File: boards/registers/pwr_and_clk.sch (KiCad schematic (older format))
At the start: 17 parts, among them J4 5V, SW1 RESET, SW2 STEP, SW3 STEP/RUN, U34 74ACT14

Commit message: Fixed some footprints
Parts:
- C37: footprint LED_SMD:LED_0805_2012Metric -> Capacitor_SMD:C_0805_2012Metric
- C38: footprint LED_SMD:LED_0805_2012Metric -> Capacitor_SMD:CP_Elec_4x4.5
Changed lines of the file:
@@
 F 0 "C38" H 9118 1396 50  0000 L CNN
 F 1 "100u" H 9118 1305 50  0000 L CNN
-F 2 "LED_SMD:LED_0805_2012Metric" H 9038 1200 50  0001 C CNN
+F 2 "Capacitor_SMD:CP_Elec_4x4.5" H 9038 1200 50  0001 C CNN
 F 3 "~" H 9000 1350 50  0001 C CNN
 	1    9000 1350
@@
 F 0 "C37" H 7665 4496 50  0000 L CNN
 F 1 "0.1u" H 7665 4405 50  0000 L CNN
-F 2 "LED_SMD:LED_0805_2012Metric" H 7588 4300 50  0001 C CNN
+F 2 "Capacitor_SMD:C_0805_2012Metric" H 7588 4300 50  0001 C CNN
 F 3 "~" H 7550 4450 50  0001 C CNN
 	1    7550 4450
@@
 	2650 2400 2650 1750
 $Comp
-L power:GND #PWR?
+L power:GND #PWR0101
 U 1 1 5FBA3876
 P 2000 3000
-F 0 "#PWR?" H 2000 2750 50  0001 C CNN
+F 0 "#PWR0101" H 2000 2750 50  0001 C CNN
 F 1 "GND" V 2005 2872 50  0000 R CNN
 F 2 "" H 2000 3000 50  0001 C CNN
@@
 $EndComp
 $Comp
-L power:GND #PWR?
+L power:GND #PWR0106
 U 1 1 5FBA3DBF
 P 2050 4400
-F 0 "#PWR?" H 2050 4150 50  0001 C CNN
+F 0 "#PWR0106" H 2050 4150 50  0001 C CNN
 F 1 "GND" V 2055 4272 50  0000 R CNN
 F 2 "" H 2050 4400 50  0001 C CNN
@@
 Connection ~ 2850 3000
 $Comp
-L power:VCC #PWR?
+L power:VCC #PWR0107
 U 1 1 5FBA8516
 P 2650 2700
-F 0 "#PWR?" H 2650 2550 50  0001 C CNN
+F 0 "#PWR0107" H 2650 2550 50  0001 C CNN
 F 1 "VCC" H 2667 2873 50  0000 C CNN
 F 2 "" H 2650 2700 50  0001 C CNN
@@
 $EndComp
 $Comp
-L power:VCC #PWR?
+L power:VCC #PWR0124
 U 1 1 5FBA8A47
 P 2850 2700
-F 0 "#PWR?" H 2850 2550 50  0001 C CNN
+F 0 "#PWR0124" H 2850 2550 50  0001 C CNN
 F 1 "VCC" H 2867 2873 50  0000 C CNN
 F 2 "" H 2850 2700 50  0001 C CNN

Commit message: Part names
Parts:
- SW3: value STEP/RUN -> OS102011MS2QN1
- U34: value 74ACT14 -> 74ACT14MTCX
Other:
- note added: "RESET"
- note added: "STEP"
- note added: "STEP/RUN"
- moved on the sheet: C37
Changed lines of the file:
@@
 P 3550 1750
 F 0 "U34" H 3550 2067 50  0000 C CNN
-F 1 "74ACT14" H 3550 1976 50  0000 C CNN
+F 1 "74ACT14MTCX" H 3550 1976 50  0000 C CNN
 F 2 "Package_SO:TSSOP-14_4.4x5mm_P0.65mm" H 3550 1750 50  0001 C CNN
 F 3 "http://www.ti.com/lit/gpn/sn74HC14" H 3550 1750 50  0001 C CNN
@@
 P 4950 1750
 F 0 "U34" H 4950 2067 50  0000 C CNN
-F 1 "74ACT14" H 4950 1976 50  0000 C CNN
+F 1 "74ACT14MTCX" H 4950 1976 50  0000 C CNN
 F 2 "Package_SO:TSSOP-14_4.4x5mm_P0.65mm" H 4950 1750 50  0001 C CNN
 F 3 "http://www.ti.com/lit/gpn/sn74HC14" H 4950 1750 50  0001 C CNN
@@
 P 5550 1750
 F 0 "U34" H 5550 2067 50  0000 C CNN
-F 1 "74ACT14" H 5550 1976 50  0000 C CNN
+F 1 "74ACT14MTCX" H 5550 1976 50  0000 C CNN
 F 2 "Package_SO:TSSOP-14_4.4x5mm_P0.65mm" H 5550 1750 50  0001 C CNN
 F 3 "http://www.ti.com/lit/gpn/sn74HC14" H 5550 1750 50  0001 C CNN
@@
 P 3550 3000
 F 0 "U34" H 3550 3317 50  0000 C CNN
-F 1 "74ACT14" H 3550 3226 50  0000 C CNN
+F 1 "74ACT14MTCX" H 3550 3226 50  0000 C CNN
 F 2 "Package_SO:TSSOP-14_4.4x5mm_P0.65mm" H 3550 3000 50  0001 C CNN
 F 3 "http://www.ti.com/lit/gpn/sn74HC14" H 3550 3000 50  0001 C CNN
@@
 P 3550 4400
 F 0 "U34" H 3550 4717 50  0000 C CNN
-F 1 "74ACT14" H 3550 4626 50  0000 C CNN
+F 1 "74ACT14MTCX" H 3550 4626 50  0000 C CNN
 F 2 "Package_SO:TSSOP-14_4.4x5mm_P0.65mm" H 3550 4400 50  0001 C CNN
 F 3 "http://www.ti.com/lit/gpn/sn74HC14" H 3550 4400 50  0001 C CNN
@@
 U 1 1 5EF35857
 P 4450 1750
-F 0 "SW3" H 4450 1425 50  0000 C CNN
-F 1 "STEP/RUN" H 4450 1516 50  0000 C CNN
+F 0 "SW3" H 4500 2000 50  0000 C CNN
+F 1 "OS102011MS2QN1" H 4250 2100 50  0000 C CNN
 F 2 "Button_Switch_THT:SW_Slide_1P2T_CK_OS102011MS2Q" H 4450 1750 50  0001 C CNN
 F 3 "~" H 4450 1750 50  0001 C CNN
@@
 P 4800 3000
 F 0 "U34" H 4800 3317 50  0000 C CNN
-F 1 "74ACT14" H 4800 3226 50  0000 C CNN
+F 1 "74ACT14MTCX" H 4800 3226 50  0000 C CNN
 F 2 "Package_SO:TSSOP-14_4.4x5mm_P0.65mm" H 4800 3000 50  0001 C CNN
 F 3 "http://www.ti.com/lit/gpn/sn74HC14" H 4800 3000 50  0001 C CNN
@@
 P 6800 4450
 F 0 "U34" H 7030 4496 50  0000 L CNN
-F 1 "74ACT14" H 7030 4405 50  0000 L CNN
+F 1 "74ACT14MTCX" H 7030 4405 50  0000 L CNN
 F 2 "Package_SO:TSSOP-14_4.4x5mm_P0.65mm" H 6800 4450 50  0001 C CNN
 F 3 "http://www.ti.com/lit/gpn/sn74HC14" H 6800 4450 50  0001 C CNN
@@
 L Device:C C37
 U 1 1 5EF50873
-P 7550 4450
-F 0 "C37" H 7665 4496 50  0000 L CNN
-F 1 "0.1u" H 7665 4405 50  0000 L CNN
-F 2 "Capacitor_SMD:C_0805_2012Metric" H 7588 4300 50  0001 C CNN
-F 3 "~" H 7550 4450 50  0001 C CNN
-	1    7550 4450
+P 7700 4450
+F 0 "C37" H 7815 4496 50  0000 L CNN
+F 1 "0.1u" H 7815 4405 50  0000 L CNN
+F 2 "Capacitor_SMD:C_0805_2012Metric" H 7738 4300 50  0001 C CNN
+F 3 "~" H 7700 4450 50  0001 C CNN
+	1    7700 4450
 	1    0    0    -1
 $EndComp
@@
 L power:GND #PWR0228
 U 1 1 5EF50EFD
-P 7550 4600
-F 0 "#PWR0228" H 7550 4350 50  0001 C CNN
-F 1 "GND" H 7555 4427 50  0000 C CNN
-F 2 "" H 7550 4600 50  0001 C CNN
-F 3 "" H 7550 4600 50  0001 C CNN
-	1    7550 4600
+P 7700 4600
+F 0 "#PWR0228" H 7700 4350 50  0001 C CNN
+F 1 "GND" H 7705 4427 50  0000 C CNN
+F 2 "" H 7700 4600 50  0001 C CNN
+F 3 "" H 7700 4600 50  0001 C CNN
+	1    7700 4600
 	1    0    0    -1
 $EndComp
@@
 L power:VCC #PWR0227
 U 1 1 5EF5151C
-P 7550 4300
-F 0 "#PWR0227" H 7550 4150 50  0001 C CNN
-F 1 "VCC" H 7567 4473 50  0000 C CNN
-F 2 "" H 7550 4300 50  0001 C CNN
-F 3 "" H 7550 4300 50  0001 C CNN
-	1    7550 4300
+P 7700 4300
+F 0 "#PWR0227" H 7700 4150 50  0001 C CNN
+F 1 "VCC" H 7717 4473 50  0000 C CNN
+F 2 "" H 7700 4300 50  0001 C CNN
+F 3 "" H 7700 4300 50  0001 C CNN
+	1    7700 4300
 	1    0    0    -1
 $EndComp
@@
 	2400 3000 2650 3000
 Connection ~ 2650 3000
+Text Notes 4550 1600 2    50   ~ 0
+STEP/RUN
+Text Notes 2300 3150 2    50   ~ 0
+RESET
+Text Notes 2350 4550 2    50   ~ 0
+STEP
 $EndSCHEMATC

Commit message: Power connector on the IO board
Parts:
- removed J4: 5V, Connector_PinHeader_2.54mm:PinHeader_1x02_P2.54mm_Vertical, symbol Connector_Generic:Conn_01x02
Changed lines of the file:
@@
-$EndComp
-$Comp
-L Connector_Generic:Conn_01x02 J4
-U 1 1 5EF4AAE6
-P 8250 1400
-F 0 "J4" H 8600 1250 50  0000 C CNN
-F 1 "5V" H 8600 1400 50  0000 C CNN
-F 2 "Connector_PinHeader_2.54mm:PinHeader_1x02_P2.54mm_Vertical" H 8250 1400 50  0001 C CNN
-F 3 "~" H 8250 1400 50  0001 C CNN
-	1    8250 1400
-	-1   0    0    1
-$EndComp
-$Comp
-L power:GND #PWR0230
-U 1 1 5EF4B86D
-P 8450 1400
-F 0 "#PWR0230" H 8450 1150 50  0001 C CNN
-F 1 "GND" H 8455 1227 50  0000 C CNN
-F 2 "" H 8450 1400 50  0001 C CNN
-F 3 "" H 8450 1400 50  0001 C CNN
-	1    8450 1400
-	1    0    0    -1
-$EndComp
-$Comp
-L power:VCC #PWR0229
-U 1 1 5EF4BF47
-P 8450 1300
-F 0 "#PWR0229" H 8450 1150 50  0001 C CNN
-F 1 "VCC" H 8467 1473 50  0000 C CNN
-F 2 "" H 8450 1300 50  0001 C CNN
-F 3 "" H 8450 1300 50  0001 C CNN
-	1    8450 1300
-	1    0    0    -1
 $EndComp
 $Comp

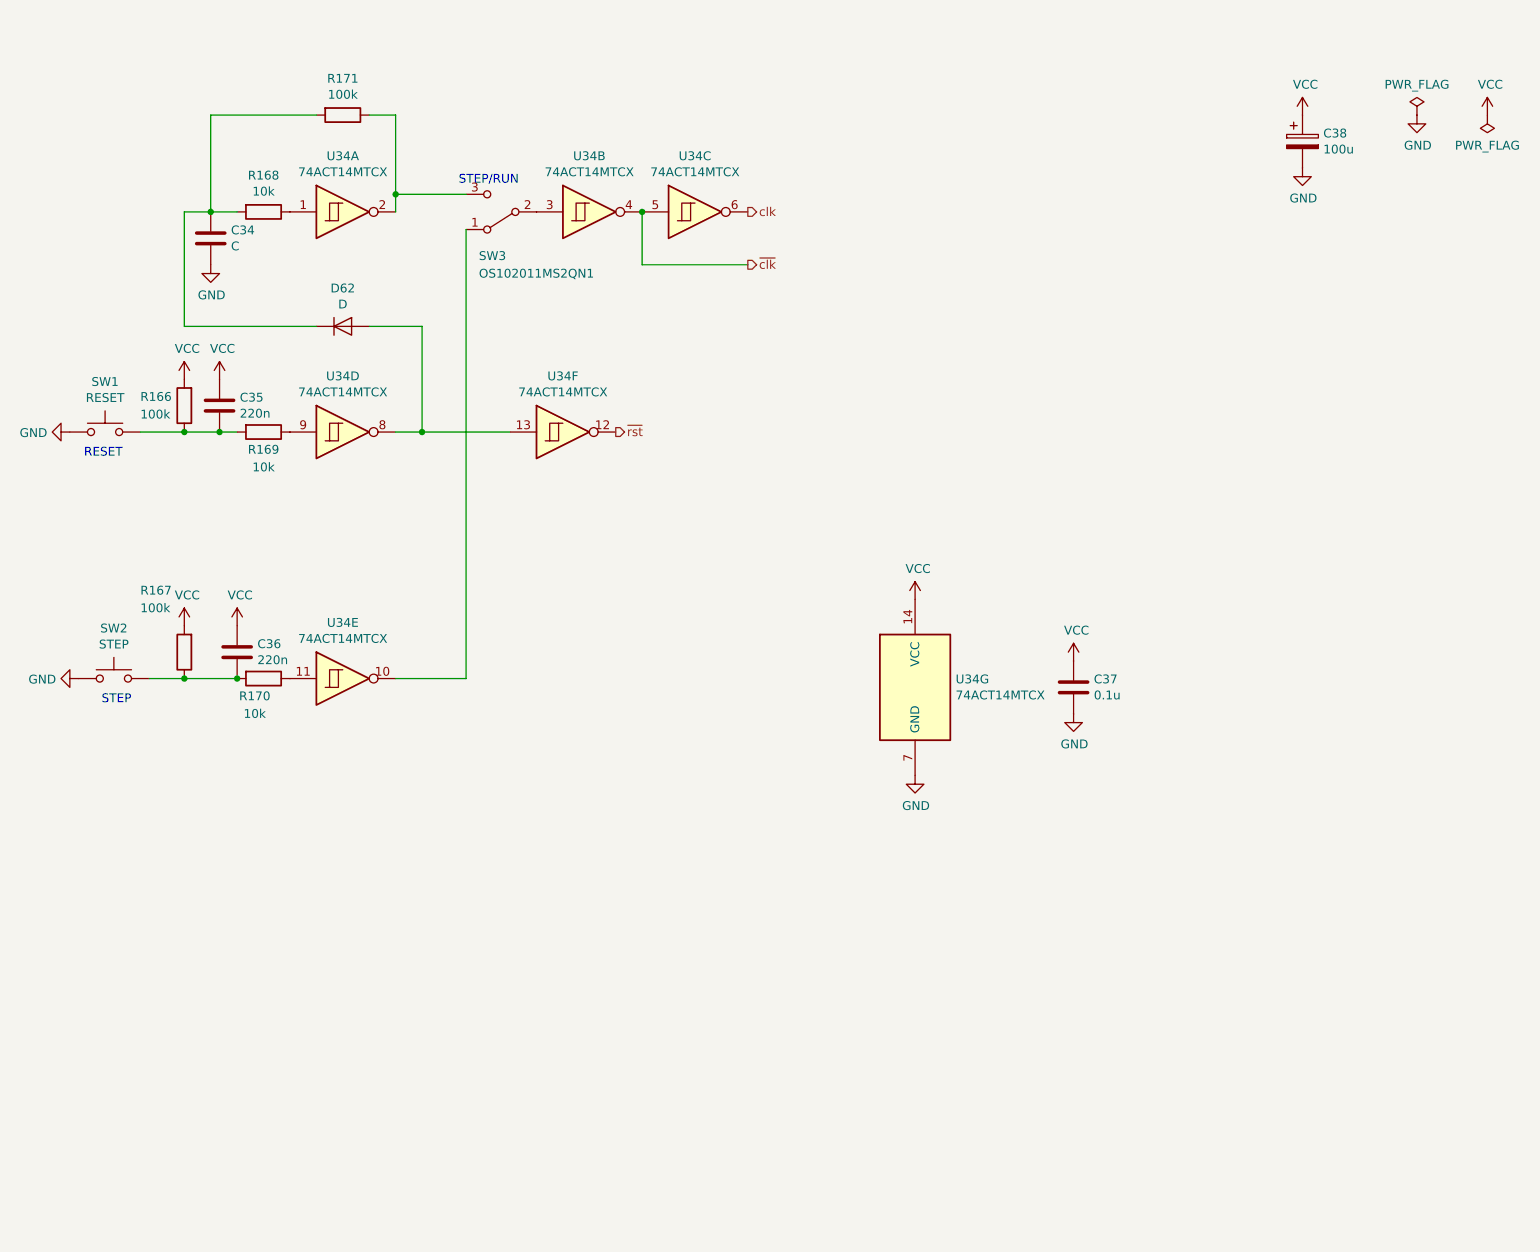
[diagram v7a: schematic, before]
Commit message: Registers: new clock and reset
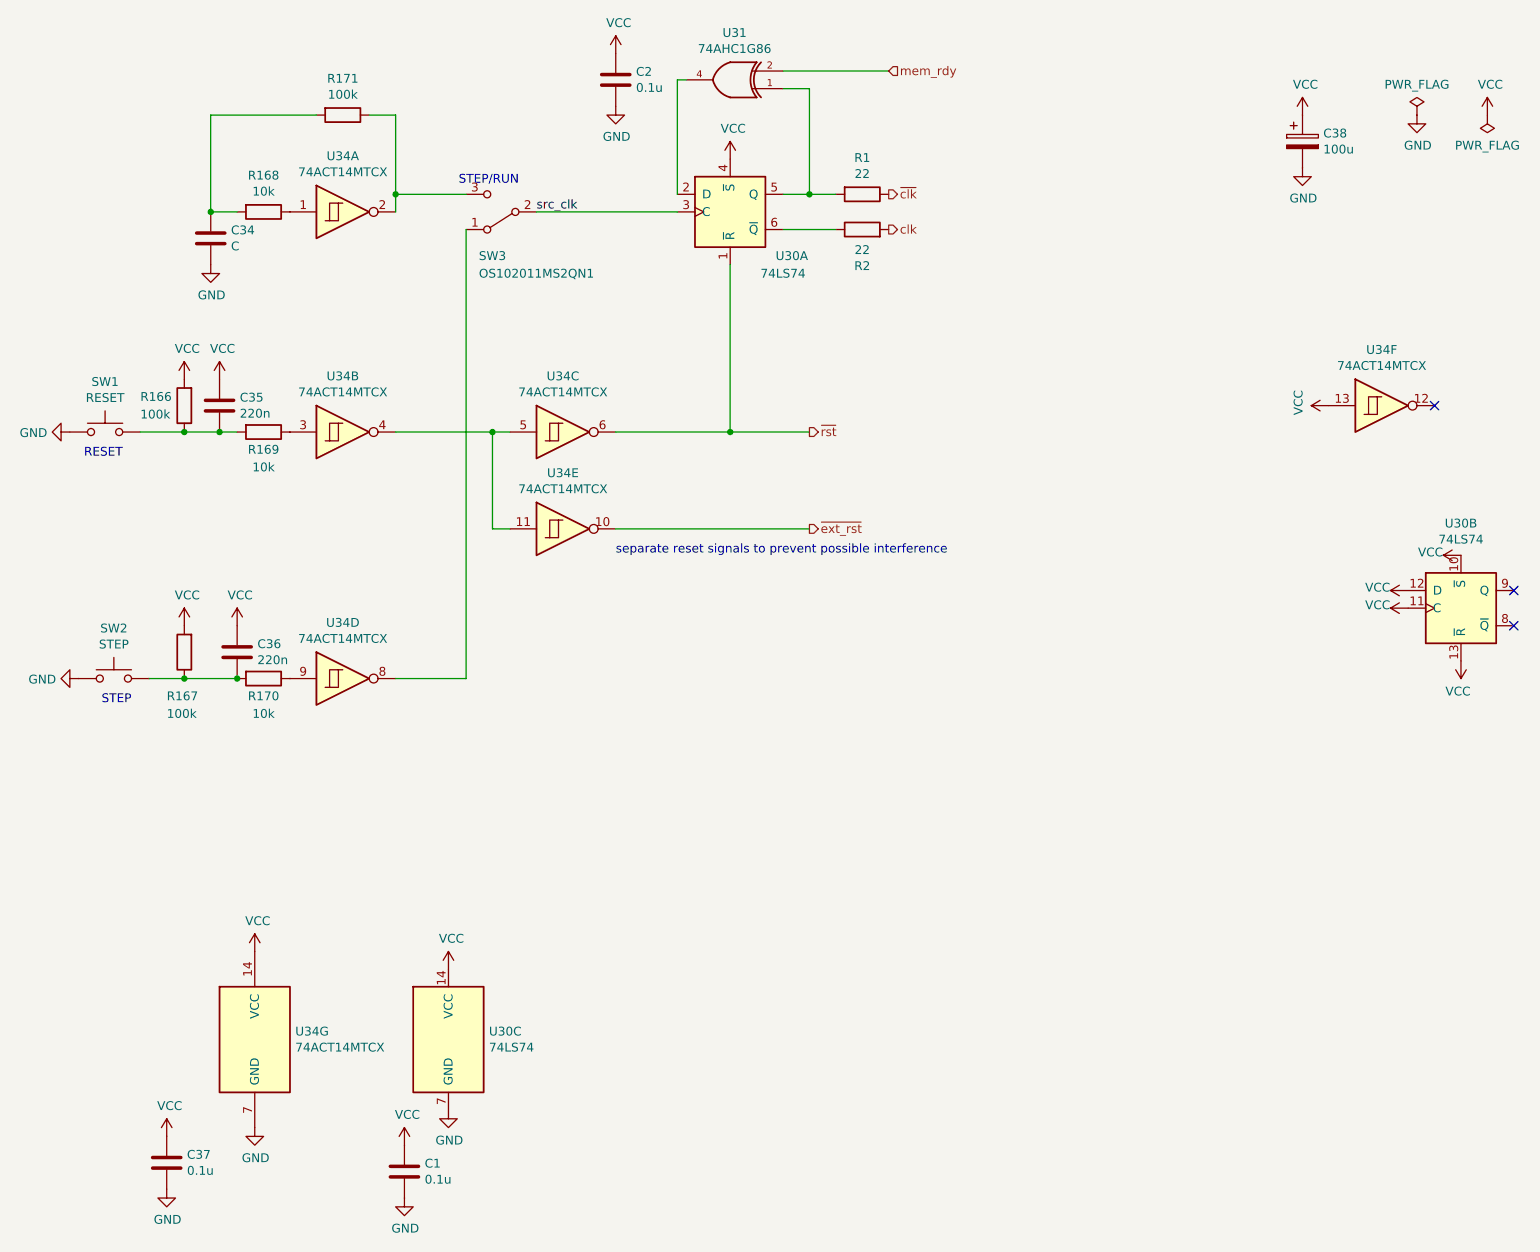
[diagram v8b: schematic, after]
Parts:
- removed D62: D, Diode_SMD:D_MiniMELF, symbol Device:D
- added C1, C2: 0.1u, Capacitor_SMD:C_0805_2012Metric, symbol Device:C
- added R1, R2: 22, Resistor_SMD:R_0805_2012Metric, symbol Device:R
- added U30: 74LS74, symbol 74xx:74LS74
- added U31: 74AHC1G86, symbol 74xGxx:74AHC1G86
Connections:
- net GND: now also C1.2, C2.2, U30.7 (GND), U31.3 (GND)
- net VCC: now also U34.13, C1.1, C2.1, U30.10 (~S), U30.11 (C), U30.12 (D), U30.13 (~R), U30.14 (VCC), U30.4 (~S), U31.5 (VCC)
- net clk: now also R2.2; no longer U34.6
- net ~clk: now also R1.1; no longer U34.4, U34.5
- net ~rst: now also U34.6, U30.1 (~R); no longer U34.12
- net at U34.3: now also R169.1; no longer SW3.2 (B)
- net at U34.9: now also R170.1; no longer R169.1
- net at U34.8: now also SW3.1 (A); no longer U34.13
- net ~ext_rst: now reaches U34.10
- net ~ext_rst: no longer SW3.1 (A)
- net at U34.11: now also U34.4, U34.5; no longer R170.1
- new net: U30.2 (D), U31.4
- new net: R1.2, U30.5 (Q), U31.1
- new net: R2.1, U30.6 (~Q)
- new net mem_rdy: U31.2
- new net src_clk: SW3.2 (B), U30.3 (C)
- no-connect marks 0 -> 3
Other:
- note added: "separate reset signals to prevent possible interference"
- moved on the sheet: C37, U34B, U34C, U34D, U34E, U34F, U34G
